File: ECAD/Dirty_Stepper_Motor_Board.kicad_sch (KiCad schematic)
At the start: 23 parts, among them J1 PWR_IN, J2 MTR_CTRL_IN, J3 SPI, M1 17HS4412B, U1 DRV8461SPWP

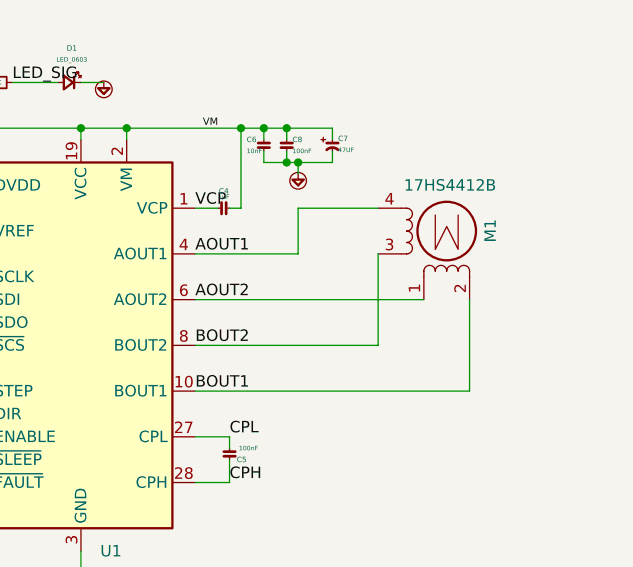
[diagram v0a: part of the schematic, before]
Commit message: Added stitching vias
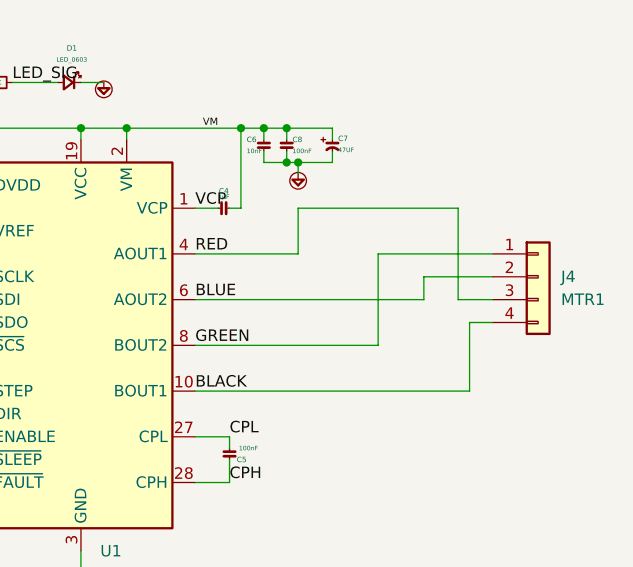
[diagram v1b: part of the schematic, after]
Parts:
- removed M1: 17HS4412B, MTA:MTA-4, symbol Motor:Stepper_Motor_bipolar
- added J4: MTR1, MTA:MTA-4, symbol Connector_Generic:Conn_01x04
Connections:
- net AOUT1 renamed RED
- net RED: now also J4.3 (Pin_3)
- net AOUT2 renamed BLUE
- net BLUE: now also J4.2 (Pin_2)
- net BOUT1 renamed BLACK
- net BLACK: now also J4.4 (Pin_4)
- net BOUT2 renamed GREEN
- net GREEN: now also J4.1 (Pin_1)
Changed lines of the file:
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@@
 	(wire
 		(pts
-			(xy 114.3 63.5) (xy 123.19 63.5)
+			(xy 114.3 63.5) (xy 132.08 63.5)
 		)
 		(stroke
@@
 	(wire
 		(pts
+			(xy 102.87 83.82) (xy 133.35 83.82)
+		)
+		(stroke
+			(width 0)
+			(type default)
+		)
+	)
+	(wire
+		(pts
 			(xy 82.55 49.53) (xy 87.63 49.53)
 		)
@@
 	(wire
 		(pts
+			(xy 123.19 68.58) (xy 135.89 68.58)
+		)
+		(stroke
+			(width 0)
+			(type default)
+		)
+	)
+	(wire
+		(pts
 			(xy 76.2 83.82) (xy 77.47 83.82)
 		)
@@
 	(wire
 		(pts
+			(xy 128.27 71.12) (xy 128.27 73.66)
+		)
+		(stroke
+			(width 0)
+			(type default)
+		)
+	)
+	(wire
+		(pts
 			(xy 48.26 77.47) (xy 53.34 77.47)
 		)
@@
 	(wire
 		(pts
+			(xy 132.08 73.66) (xy 135.89 73.66)
+		)
+		(stroke
+			(width 0)
+			(type default)
+		)
+	)
+	(wire
+		(pts
+			(xy 128.27 71.12) (xy 135.89 71.12)
+		)
+		(stroke
+			(width 0)
+			(type default)
+		)
+	)
+	(wire
+		(pts
 			(xy 48.26 72.39) (xy 62.23 72.39)
 		)
@@
 	(wire
 		(pts
+			(xy 132.08 63.5) (xy 132.08 73.66)
+		)
+		(stroke
+			(width 0)
+			(type default)
+		)
+	)
+	(wire
+		(pts
 			(xy 48.26 97.79) (xy 53.34 97.79)
 		)
@@
 	(wire
 		(pts
-			(xy 133.35 83.82) (xy 102.87 83.82)
+			(xy 78.74 54.61) (xy 90.17 54.61)
 		)
 		(stroke
@@
 	(wire
 		(pts
-			(xy 78.74 54.61) (xy 90.17 54.61)
+			(xy 133.35 76.2) (xy 135.89 76.2)
 		)
 		(stroke
@@
 	(wire
 		(pts
-			(xy 133.35 73.66) (xy 133.35 83.82)
+			(xy 133.35 76.2) (xy 133.35 83.82)
 		)
 		(stroke
@@
 		)
 	)
-	(label "AOUT1"
+	(label "RED"
 		(at 102.87 68.58 0)
 		(effects
@@
 		)
 	)
-	(label "BOUT2"
+	(label "GREEN"
 		(at 102.87 78.74 0)
 		(effects
@@
 		)
 	)
-	(label "AOUT2"
+	(label "BLUE"
 		(at 102.87 73.66 0)
 		(effects
@@
 		)
 	)
-	(label "BOUT1"
+	(label "BLACK"
 		(at 102.87 83.82 0)
 		(effects
@@
 	)
 	(symbol
-		(lib_id "Motor:Stepper_Motor_bipolar")
-		(at 130.81 66.04 0)
-		(mirror x)
-		(unit 1)
-		(body_style 1)
-		(exclude_from_sim no)
-		(in_bom yes)
-		(on_board yes)
-		(in_pos_files yes)
-		(dnp no)
-		(property "Reference" "M1"
-			(at 135.6742 67.31 90)
-			(show_name no)
-			(do_not_autoplace no)
-			(effects
-				(font
-					(size 1.27 1.27)
-				)
-				(justify right)
-			)
-		)
-		(property "Value" "17HS4412B"
-			(at 136.3092 60.96 0)
-			(show_name no)
-			(do_not_autoplace no)
-			(effects
-				(font
-					(size 1.27 1.27)
-				)
-				(justify right)
-			)
-		)
-		(property "Footprint" "MTA:MTA-4"
-			(at 131.064 65.786 0)
-			(hide yes)
-			(show_name no)
-			(do_not_autoplace no)
-			(effects
-				(font
-					(size 1.27 1.27)
-				)
-			)
-		)
-		(property "Datasheet" "http://www.infineon.com/dgdl/Application-Note-TLE8110EE_driving_UniPolarStepperMotor_V1.1.pdf?fileId=db3a30431be39b97011be5d0aa0a00b0"
-			(at 131.064 65.786 0)
-			(hide yes)
-			(show_name no)
-			(do_not_autoplace no)
-			(effects
-				(font
-					(size 1.27 1.27)
-				)
-			)
-		)
-		(property "Description" "4-wire bipolar stepper motor"
-			(at 130.81 66.04 0)
-			(hide yes)
-			(show_name no)
-			(do_not_autoplace no)
-			(effects
-				(font
-					(size 1.27 1.27)
-				)
-			)
-		)
-		(pin "3"
-		)
-		(pin "2"
-		)
-		(pin "4"
-		)
-		(pin "1"
-		)
-		(instances
-			(project "Dirty_Stepper_Motor_Board"
-				(path "/e2108898-a7cf-4afc-a0ee-7ef80a7e9bd5"
-					(reference "M1")
-					(unit 1)
-				)
-			)
-		)
-	)
-	(symbol
 		(lib_id "PWR_MANAGEMENT:V-GND")
 		(at 55.88 63.5 0)
@@
 					(unit 1)
 				)
+			)
+		)
+	)
+	(symbol
+		(lib_id "Connector_Generic:Conn_01x04")
+		(at 140.97 71.12 0)
+		(unit 1)
+		(body_style 1)
+		(exclude_from_sim no)
+		(in_bom yes)
+		(on_board yes)
+		(in_pos_files yes)
+		(dnp no)
+		(fields_autoplaced yes)
+		(property "Reference" "J4"
+			(at 143.51 71.1199 0)
+			(show_name no)
+			(do_not_autoplace no)
+			(effects
+				(font
+					(size 1.27 1.27)
+				)
+				(justify left)
+			)
+		)
+		(property "Value" "MTR1"
+			(at 143.51 73.6599 0)
+			(show_name no)
+			(do_not_autoplace no)
+			(effects
+				(font
+					(size 1.27 1.27)
+				)
+				(justify left)
+			)
+		)
+		(property "Footprint" "MTA:MTA-4"
+			(at 140.97 71.12 0)
+			(hide yes)
+			(show_name no)
+			(do_not_autoplace no)
+			(effects
+				(font
+					(size 1.27 1.27)
+				)
+			)
+		)
+		(property "Datasheet" ""
+			(at 140.97 71.12 0)
+			(hide yes)
+			(show_name no)
+			(do_not_autoplace no)
+			(effects
+				(font
+					(size 1.27 1.27)
+				)
+			)
+		)
+		(property "Description" "Generic connector, single row, 01x04, script generated (kicad-library-utils/schlib/autogen/connector/)"
+			(at 140.97 71.12 0)
+			(hide yes)
+			(show_name no)
+			(do_not_autoplace no)
+			(effects
+				(font
+					(size 1.27 1.27)
+				)
+			)
+		)
+		(pin "4"
+		)
+		(pin "3"
+		)
+		(pin "2"
+		)
+		(pin "1"
+		)
+		(instances
+			(project "Dirty_Stepper_Motor_Board"
+				(path "/e2108898-a7cf-4afc-a0ee-7ef80a7e9bd5"
+					(reference "J4")
+					(unit 1)
+				)
